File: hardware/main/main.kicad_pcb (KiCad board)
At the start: 4 copper layers, 75 x 50 mm, 112 parts, among them IC1 ICM-42688-P, IC10 PE64906B-Z, IC2 PAM2306DYPAA, IC3 CC1121RHBR, IC4 CC1190RGVR, IC5 TXE8116DGSR, IC6 PE64906B-Z, IC7 PE64906B-Z, IC8 PE64906B-Z, IC9 PE64906B-Z, J1 USB-C, J10 Conn_01x08_Pin, J2 Conn_01x08_Pin, J3 Conn_01x03_Pin, J4 Conn_01x09, J5 Conn_01x08_Pin, J6 Conn_01x01, J7 Conn_01x08_Pin, J8 Conn_01x08_Pin, J9 Conn_01x08_Pin, SW1 SW_Push, SW2 SW_Push, U1 RP2354B, U2 LSM6DSO32, U3 LG77LICMD, U4 LPS22DF, Y1 12MHz, Y2 32MHz

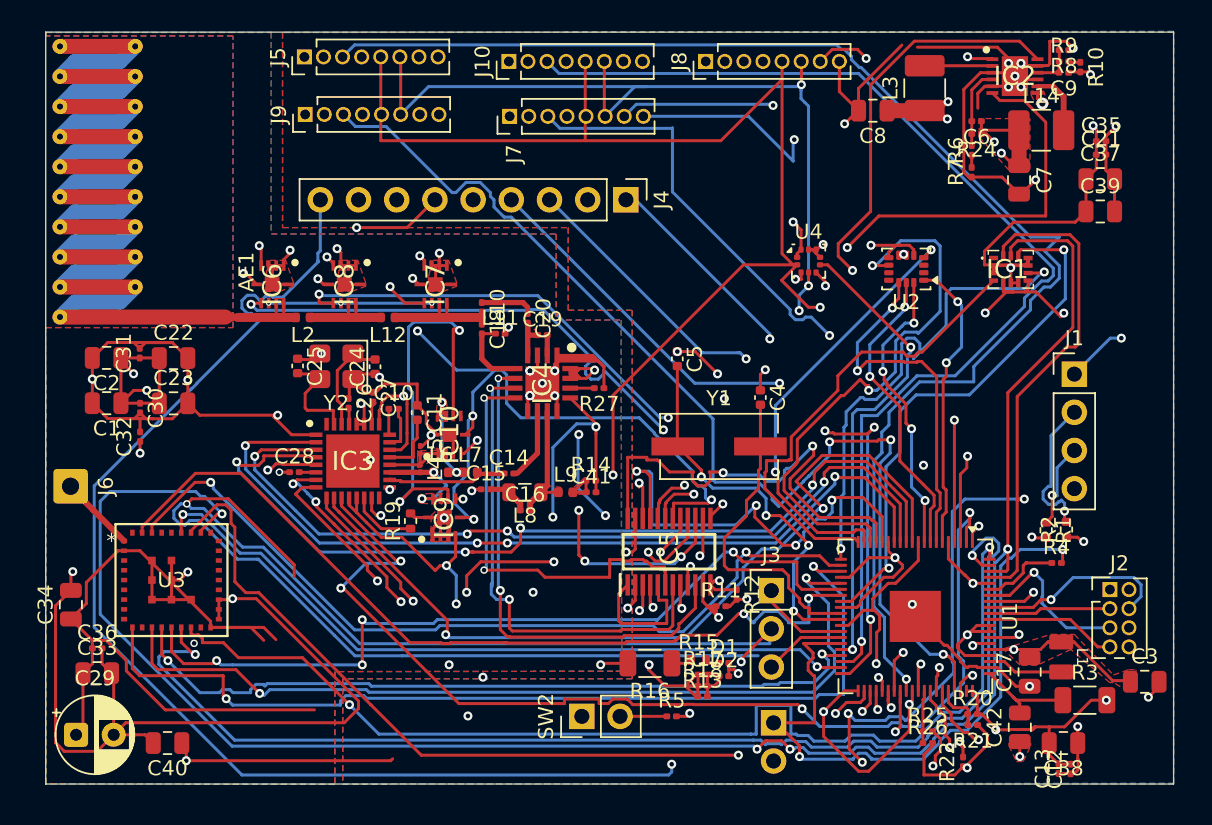
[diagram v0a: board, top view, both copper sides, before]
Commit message: main: enforce standard fab rules and clean routed board
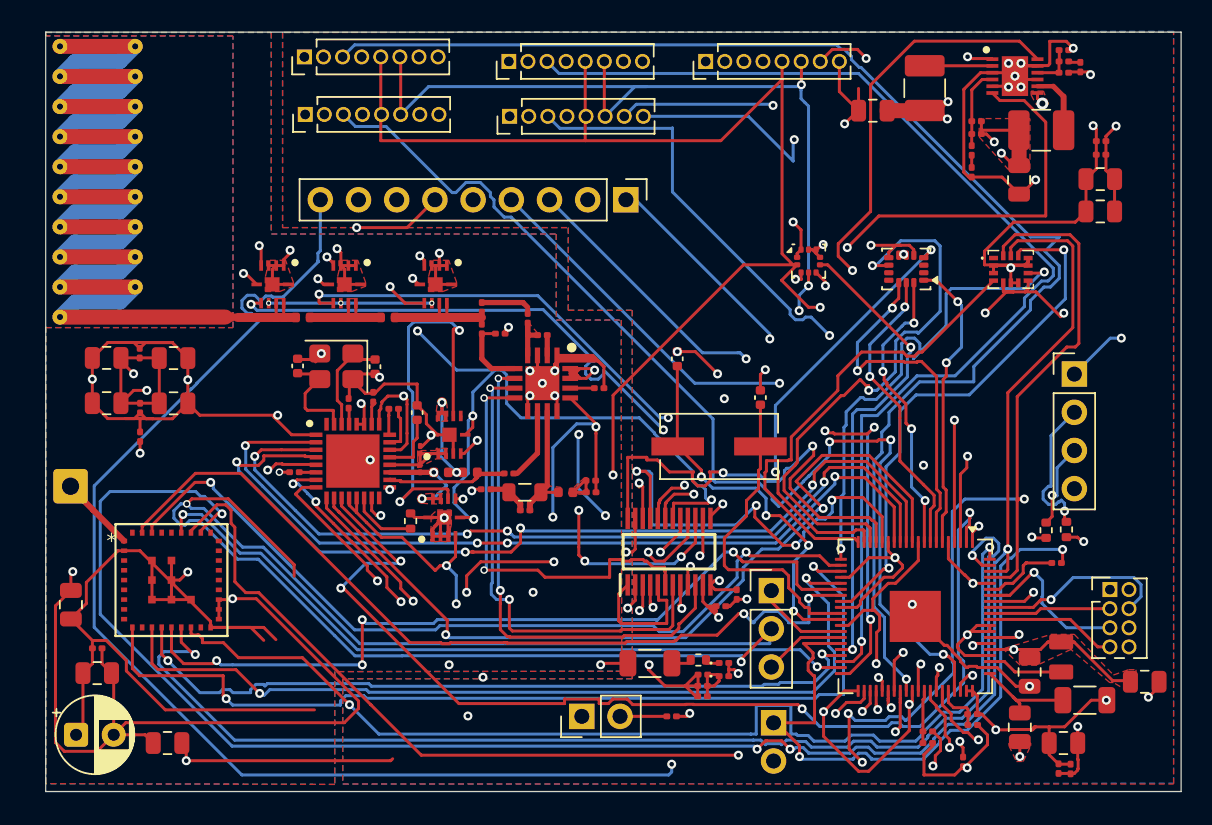
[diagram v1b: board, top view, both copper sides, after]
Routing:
- net GND: track 873.8 -> 860.0 mm, vias 55 -> 52
- net Net-(U1-RUN): track 61.8 -> 60.5 mm
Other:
- board size 75 x 50 mm -> 75.5 x 50.5 mm
